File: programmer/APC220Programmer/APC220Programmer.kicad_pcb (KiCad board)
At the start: 2 copper layers, 109.9 x 55 mm, 14 parts, among them Q1 2N7000, SW1 SW_SPST, SW2 Rotary_Encoder_Switch, U1 Adafruit BMP390 Module, U2 MPXH6115A6U/T1

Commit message: Minor improvements
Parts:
- BT1: footprint Connector_PinHeader_2.54mm:PinHeader_1x02_P2.54mm_Vertical -> Connector_Molex:Molex_KK-254_AE-6410-02A_1x02_P2.54mm_Vertical
- moved BT1 3.61 mm to (171.1, 123.9), turned to 180 degrees
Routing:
- net Net-(BT1-+): track 4.95 -> 10.6 mm
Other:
- board text added: "9V - +"
- board text added: "https://github.com/emcgon/APC-Tools Revision ${REVISION}"
- board text removed: "9V + -"
- board text removed: "https://github.com/emcgon/APC-Tools"

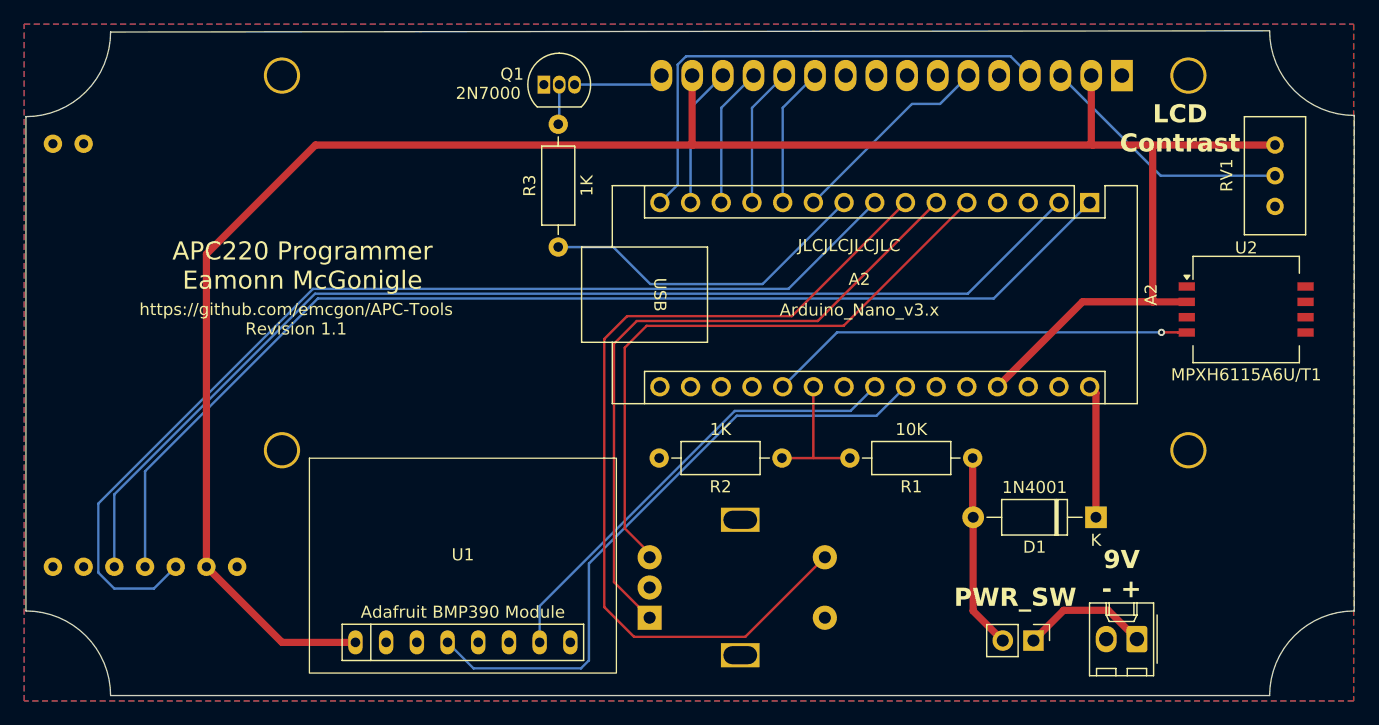
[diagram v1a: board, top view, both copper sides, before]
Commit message: Added current-limiting resistor for display backlight. Replaced rounded corners with square corners
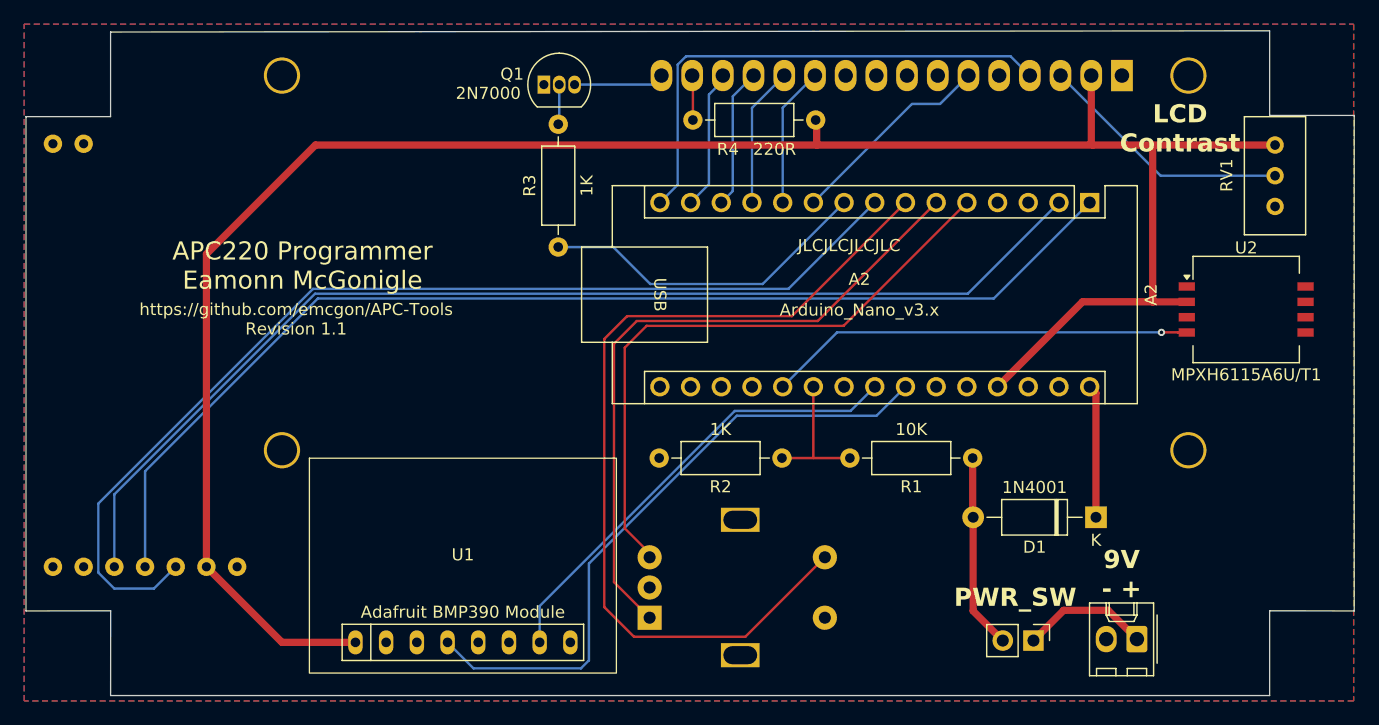
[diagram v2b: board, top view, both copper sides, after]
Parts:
- added R4: 220R, Resistor_THT:R_Axial_DIN0207_L6.3mm_D2.5mm_P10.16mm_Horizontal, F.Cu at (134.3, 80.9)
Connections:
- DS1 pad 15: +5V -> Net-(DS1-LED(+))
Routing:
- net Net-(DS1-LED(+)): track 0.00 -> 3.70 mm
- net +5V: track 176.0 -> 172.4 mm
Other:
- outline, holes or cut-outs redrawn
